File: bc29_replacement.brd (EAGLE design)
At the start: 160 x 100 mm, 4 parts, among them IC1 ATMEGA328P, IC17 CD4070B, J2 2520-5

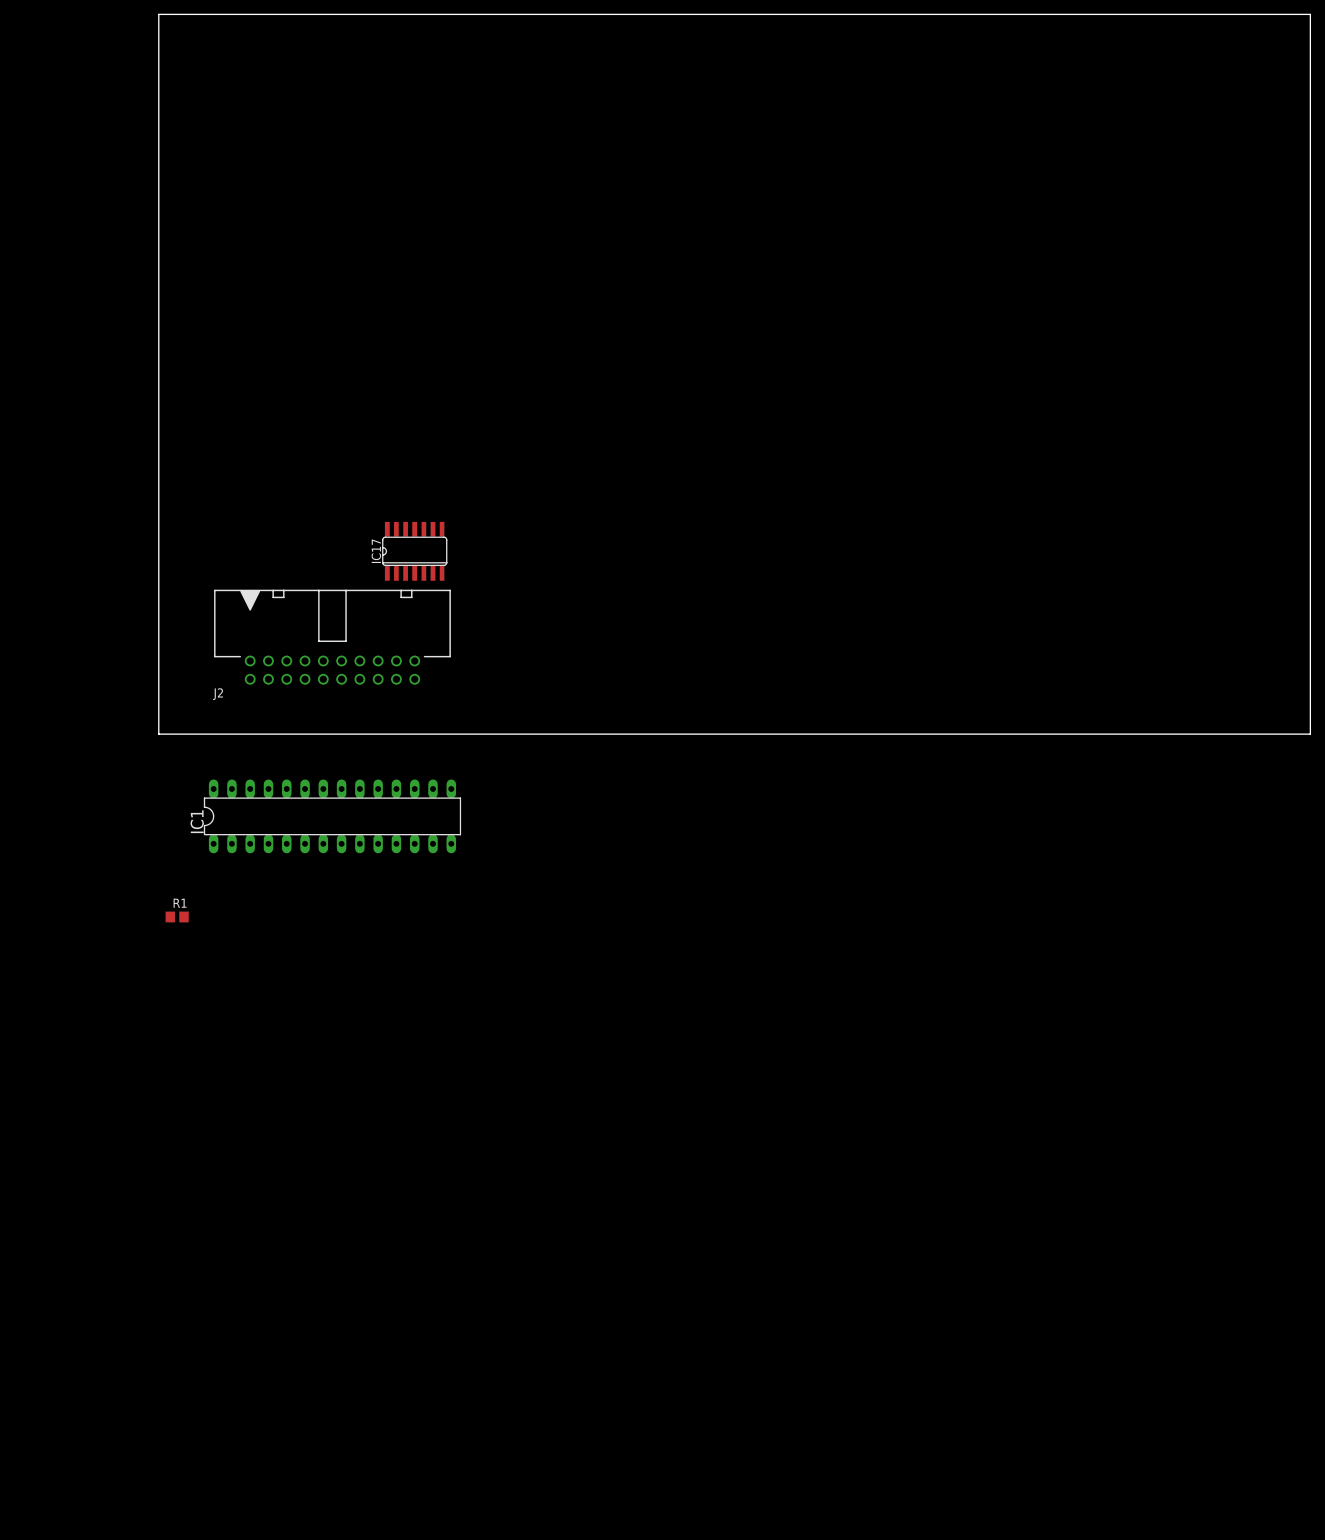
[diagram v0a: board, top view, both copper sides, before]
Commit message: MCU and PCB dimensions
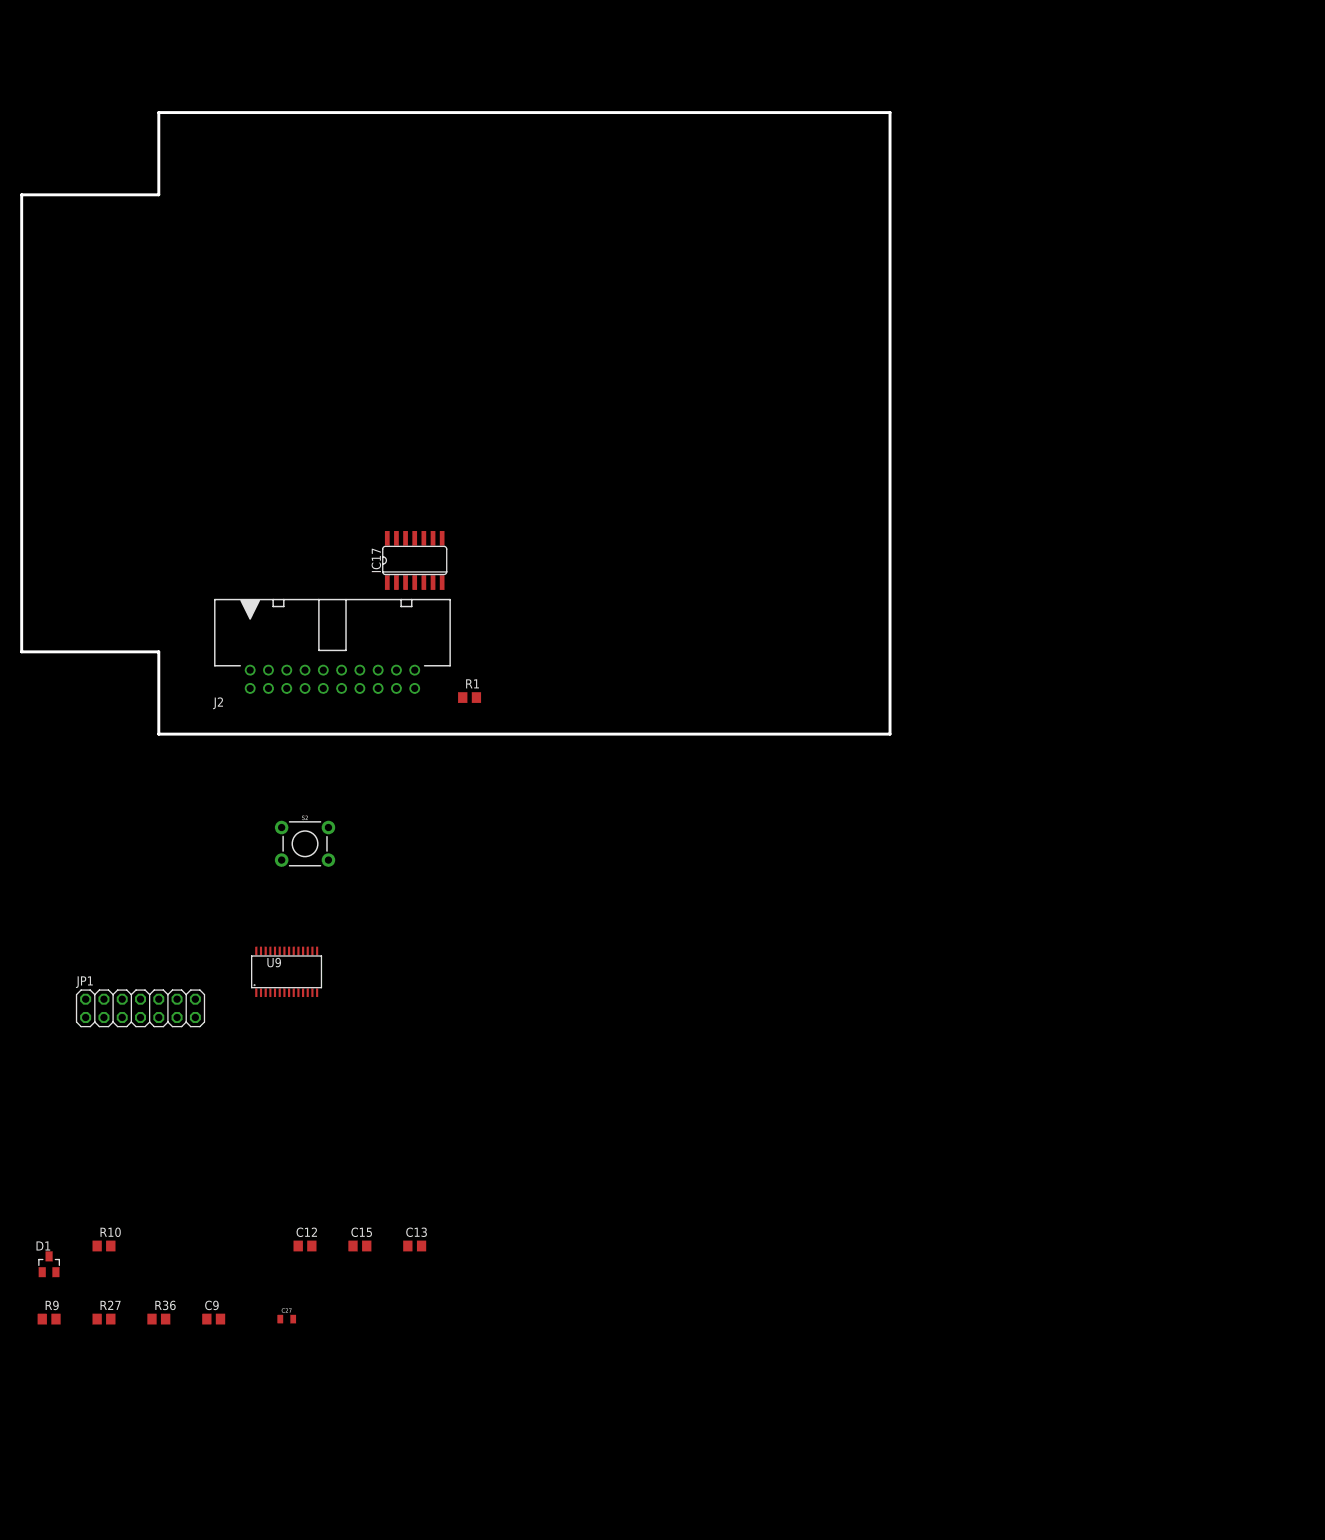
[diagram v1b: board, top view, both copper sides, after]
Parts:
- removed IC1: ATMEGA328P, adafruit:DIL28-3
- added C12: .47uF, rcl:C0805
- added C13: 10uF, rcl:C0805
- added C15: 2.2nF, rcl:C0805
- added C27: 0.1u, SparkFun-Capacitors:0805
- added C9: .1uF, rcl:C0805
- added D1: BAT54, diode:SOT23
- added JP1: JTAG, pinhead:2X07
- added R10: 20.0K, rcl:R0805
- added R27: 0R0, rcl:R0805
- added R36: 300, rcl:R0805
- added R9: 47K, rcl:R0805
- added S2: SPST-PTH-6.0MM, SparkFun-Switches:TACTILE_SWITCH_PTH_6.0MM
- added U9: MSP430I2041TPW, TI_MSP430_v16:PW28
- moved R1 50.8 mm to (43.2, 5.08)
- moved J2 1.27 mm to (24.1, 7.62)
- moved IC17 1.27 mm to (35.6, 24.1)
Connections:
- new net A0.0+: U9.1
- new net A0.0-: U9.2
- new net A1.0+: U9.3
- new net A1.0-: U9.4
- new net A2.0+: U9.5
- new net A2.0-: U9.6
- new net A3.0+: U9.7
- new net A3.0-: U9.8
- new net AGND: C27.2, R10.2, R27.2, U9.10
- new net P1.0: U9.17
- new net P1.1: U9.18
- new net P1.4: U9.21
- new net P1.5: U9.22
- new net P1.6: U9.23
- new net P1.7: U9.24
- new net P2.0: U9.25
- new net P2.1: U9.26
- new net P2.2: U9.27
- new net P2.3: U9.28
- new net ROSC: R10.1, U9.11
- new net RST_JTAG: C15.2, JP1.1, R36.1, R9.1, U9.15
- new net RST_PB: R36.2, S2.3
- new net SBWTCK: JP1.7, U9.16
- new net UCA0RXD: JP1.14, U9.19
- new net UCA0TXD: JP1.12, U9.20
- new net VCC: C13.2, C9.1, D1.3, R9.2, U9.13
- new net VCC_JTAG: D1.1, JP1.2
- new net VCORE: C12.2, U9.14
- new net VREF: C27.1, U9.9
- net GND: now also C12.1, C13.1, C15.1, C9.2, JP1.9, R27.1, S2.1, U9.12
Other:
- board size 160 x 100 mm -> 120.6 x 86.4 mm

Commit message: input network
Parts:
- added C1: 100nF, rcl:C1206
- added C19, C21: 10nF, rcl:C0805
- added C2: 33uF 450V, rcl:E7,5-18
- added C3, C4, C5: 47pF, rcl:C0805
- added D2: P6KEXXC, diode:CB417-15
- added D8: 1N4448, diode:MINIMELF
- added D9: 1N4004, diode:SOD80C
- added E2: 10uF 63V, rcl:E2,5-5
- added E3: 47uf 25V, rcl:E2,5-5
- added F1: 32mA, fuse:FUSE_HOLDER_5X20MM
- added IC18: LP2951, linear:SO08
- added L1: 8mH, inductor-neosid:Z15/4
- added L2, L3: (no value), inductor-neosid:SM-B9
- added M1: IRF740, transistor-power:TO220BV
- added R2, R3: 1.0K, rcl:R0805
- added R29, R30: 1M, rcl:M0805
- added X1: 236-412, con-wago-508:236-412
- added Z1: 12V, diode:SOD80C
- added Z2: 6.2V, diode:SOD80C
- J2: value 2520-5 -> 2520-; device con-3m:PAK100/2500-5-20 -> con-3m:PAK100/2500-20
- moved C12 136.0 mm to (97.8, 40.6)
- moved C13 136.0 mm to (113.0, 40.6)
- moved C15 136.0 mm to (105.4, 40.6)
- moved C27 136.0 mm to (95.2, 30.5)
- moved C9 136.0 mm to (85.1, 30.5)
- moved R10 136.0 mm to (69.8, 40.6)
- moved R27 136.0 mm to (69.8, 30.5)
- moved R36 136.0 mm to (77.5, 30.5)
- moved R9 136.0 mm to (62.2, 30.5)
- moved D1 136.0 mm to (62.2, 38.1)
- moved JP1 136.0 mm to (74.9, 73.7)
- moved U9 136.0 mm to (95.2, 78.7)
- moved S2 75.1 mm to (85.1, 22.9)
- moved J2 22.9 mm to (31.8, 29.2), turned to 90 degrees
- moved IC17 19.0 mm to (54.6, 24.1)
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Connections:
- new net !NAR: X1.5@1
- new net !RESET: X1.7@1
- new net +BATT: F1.1, L1.1, X1.1@1
- new net +BATT_FILT: C2.+, L1.2
- new net 12+: X1.11@1
- new net 12-: X1.12@1
- new net 13V5: D8.A, E2.+, IC18.8, M1.S
- new net AH_NEGATIVE: X1.8@1
- new net DRAIN: D9.C, M1.D
- new net FUSED_BATT+: D9.A, F1.2, R30.2
- new net GATE: C21.1, D8.C, M1.G, R29.2, Z1.C
- new net GND1K: X1.6@1
- new net N$1: D2.C, L2.1
- new net N$2: D2.A, L3.1
- new net N$29: R29.1, R30.1
- new net N$44: IC18.6, IC18.7
- new net N$5: L2.2, R2.2
- new net N$8: L3.2, R3.2
- new net OUT+: X1.9@1
- new net OUT-: X1.10@1
- new net SHUNT+: X1.4@1
- new net SHUNT-: X1.3@1
- net +5V: now also C1.1, C19.1, E3.+, IC18.1, IC18.2, Z1.A, Z2.C
- net A0.0+: now also C4.1, C5.1, R3.1
- net A0.0-: now also C3.2, C5.2, R2.1
- net GND: now also C1.2, C19.2, C2.-, C21.2, C3.1, C4.2, E2.-, E3.-, IC18.4, X1.2@1, Z2.A
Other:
- board size 120.6 x 86.4 mm -> 120.7 x 86.4 mm

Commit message: io expansion
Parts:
- added IC1: 74HCS596D, 74xx-us:SO16
- moved C3 163.5 mm to (108.0, 27.9)
- moved C4 163.5 mm to (108.0, 15.2)
- moved C5 163.5 mm to (108.0, 8.89)
- moved R2 163.5 mm to (108.0, 34.3)
- moved R3 163.5 mm to (108.0, 21.6)
- moved L3 114.1 mm to (95.2, 7.62)
- moved L2 113.1 mm to (94.0, 12.7)
- moved D2 112.5 mm to (96.5, 3.81)
- moved C2 101.1 mm to (33.0, 67.3)
- moved L1 66.3 mm to (27.9, 54.6)
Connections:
- net GND: now also IC1.8
- net VCC: now also IC1.16
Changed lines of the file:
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@@
 <attribute name="MF" value="Wago Corporation" x="6.35" y="71.12" size="1.778" layer="27" rot="R270" display="off"/>
 </element>
-<element name="L1" library="inductor-neosid" package="Z15/4" value="8mH" x="5.08" y="-7.62">
-<attribute name="OC_NEWARK" value="unknown" x="5.08" y="-7.62" size="1.778" layer="27" display="off"/>
-<attribute name="OC_FARNELL" value="unknown" x="5.08" y="-7.62" size="1.778" layer="27" display="off"/>
-<attribute name="MPN" value="" x="5.08" y="-7.62" size="1.778" layer="27" display="off"/>
-<attribute name="MF" value="" x="5.08" y="-7.62" size="1.778" layer="27" display="off"/>
+<element name="L1" library="inductor-neosid" package="Z15/4" value="8mH" x="27.94" y="54.61">
+<attribute name="OC_NEWARK" value="unknown" x="27.94" y="54.61" size="1.778" layer="27" display="off"/>
+<attribute name="OC_FARNELL" value="unknown" x="27.94" y="54.61" size="1.778" layer="27" display="off"/>
+<attribute name="MPN" value="" x="27.94" y="54.61" size="1.778" layer="27" display="off"/>
+<attribute name="MF" value="" x="27.94" y="54.61" size="1.778" layer="27" display="off"/>
 </element>
-<element name="C2" library="rcl" package="E7,5-18" value="33uF 450V" x="12.7" y="-31.75"/>
-<element name="L2" library="inductor-neosid" package="SM-B9" value="" x="1.27" y="-52.07">
-<attribute name="OC_NEWARK" value="unknown" x="1.27" y="-52.07" size="1.778" layer="27" display="off"/>
-<attribute name="OC_FARNELL" value="unknown" x="1.27" y="-52.07" size="1.778" layer="27" display="off"/>
-<attribute name="MPN" value="" x="1.27" y="-52.07" size="1.778" layer="27" display="off"/>
-<attribute name="MF" value="" x="1.27" y="-52.07" size="1.778" layer="27" display="off"/>
+<element name="C2" library="rcl" package="E7,5-18" value="33uF 450V" x="33.02" y="67.31"/>
+<element name="L2" library="inductor-neosid" package="SM-B9" value="" x="93.98" y="12.7">
+<attribute name="OC_NEWARK" value="unknown" x="93.98" y="12.7" size="1.778" layer="27" display="off"/>
+<attribute name="OC_FARNELL" value="unknown" x="93.98" y="12.7" size="1.778" layer="27" display="off"/>
+<attribute name="MPN" value="" x="93.98" y="12.7" size="1.778" layer="27" display="off"/>
+<attribute name="MF" value="" x="93.98" y="12.7" size="1.778" layer="27" display="off"/>
 </element>
-<element name="L3" library="inductor-neosid" package="SM-B9" value="" x="1.27" y="-57.15">
-<attribute name="OC_NEWARK" value="unknown" x="1.27" y="-57.15" size="1.778" layer="27" display="off"/>
-<attribute name="OC_FARNELL" value="unknown" x="1.27" y="-57.15" size="1.778" layer="27" display="off"/>
-<attribute name="MPN" value="" x="1.27" y="-57.15" size="1.778" layer="27" display="off"/>
-<attribute name="MF" value="" x="1.27" y="-57.15" size="1.778" layer="27" display="off"/>
+<element name="L3" library="inductor-neosid" package="SM-B9" value="" x="95.25" y="7.62">
+<attribute name="OC_NEWARK" value="unknown" x="95.25" y="7.62" size="1.778" layer="27" display="off"/>
+<attribute name="OC_FARNELL" value="unknown" x="95.25" y="7.62" size="1.778" layer="27" display="off"/>
+<attribute name="MPN" value="" x="95.25" y="7.62" size="1.778" layer="27" display="off"/>
+<attribute name="MF" value="" x="95.25" y="7.62" size="1.778" layer="27" display="off"/>
 </element>
-<element name="D2" library="diode" package="CB417-15" value="P6KEXXC" x="11.43" y="-69.85"/>
-<element name="C3" library="rcl" package="C0805" value="47pF" x="-5.08" y="-90.17"/>
-<element name="R2" library="rcl" package="R0805" value="1.0K " x="-5.08" y="-83.82"/>
-<element name="R3" library="rcl" package="R0805" value="1.0K " x="-5.08" y="-96.52"/>
-<element name="C4" library="rcl" package="C0805" value="47pF" x="-5.08" y="-102.87"/>
-<element name="C5" library="rcl" package="C0805" value="47pF" x="-5.08" y="-109.22"/>
+<element name="D2" library="diode" package="CB417-15" value="P6KEXXC" x="96.52" y="3.81"/>
+<element name="C3" library="rcl" package="C0805" value="47pF" x="107.95" y="27.94"/>
+<element name="R2" library="rcl" package="R0805" value="1.0K " x="107.95" y="34.29"/>
+<element name="R3" library="rcl" package="R0805" value="1.0K " x="107.95" y="21.59"/>
+<element name="C4" library="rcl" package="C0805" value="47pF" x="107.95" y="15.24"/>
+<element name="C5" library="rcl" package="C0805" value="47pF" x="107.95" y="8.89"/>
+<element name="IC1" library="74xx-us" package="SO16" value="74HCS596D" x="97.79" y="55.88"/>
 </elements>
 <signals>
@@
 <contactref element="C3" pad="1"/>
 <contactref element="C4" pad="2"/>
+<contactref element="IC1" pad="8"/>
 <wire x1="77.47" y1="72.39" x2="98.1711" y2="75.832" width="0" layer="19" extent="1-1"/>
 <wire x1="73.66" y1="68.58" x2="77.47" y2="72.39" width="0" layer="19" extent="1-1"/>
@@
 <wire x1="104.46" y1="40.64" x2="96.84" y2="40.64" width="0" layer="19" extent="1-1"/>
 <wire x1="112.08" y1="40.64" x2="104.46" y2="40.64" width="0" layer="19" extent="1-1"/>
+<wire x1="107" y1="27.94" x2="104.46" y2="40.64" width="0" layer="19" extent="1-1"/>
+<wire x1="108.9" y1="15.24" x2="107" y2="27.94" width="0" layer="19" extent="1-1"/>
 <wire x1="68.9" y1="30.48" x2="81.8388" y2="25.1206" width="0" layer="19" extent="1-1"/>
 <wire x1="58.42" y1="21.0566" x2="68.9" y2="30.48" width="0" layer="19" extent="1-1"/>
 <wire x1="50.8" y1="68.58" x2="73.66" y2="68.58" width="0" layer="19" extent="1-1"/>
+<wire x1="36.83" y1="67.31" x2="50.8" y2="68.58" width="0" layer="19" extent="1-1"/>
 <wire x1="42.86" y1="38.1" x2="58.42" y2="21.0566" width="0" layer="19" extent="1-1"/>
 <wire x1="33.02" y1="22.86" x2="42.86" y2="38.1" width="0" layer="19" extent="1-1"/>
-<wire x1="3.81" y1="66.04" x2="50.8" y2="68.58" width="0" layer="19" extent="1-1"/>
-<wire x1="16.51" y1="-31.75" x2="33.02" y2="22.86" width="0" layer="19" extent="1-1"/>
-<wire x1="-6.03" y1="-90.17" x2="16.51" y2="-31.75" width="0" layer="19" extent="1-1"/>
-<wire x1="-4.13" y1="-102.87" x2="-6.03" y2="-90.17" width="0" layer="19" extent="1-1"/>
+<wire x1="3.81" y1="66.04" x2="36.83" y2="67.31" width="0" layer="19" extent="1-1"/>
+<wire x1="102.235" y1="52.8066" x2="33.02" y2="22.86" width="0" layer="19" extent="1-1"/>
 </signal>
 <signal name="+5V">
@@
 <contactref element="R9" pad="2"/>
 <contactref element="D1" pad="3"/>
+<contactref element="IC1" pad="16"/>
+<wire x1="113.98" y1="40.64" x2="98.8211" y2="75.832" width="0" layer="19" extent="1-1"/>
+<wire x1="84.14" y1="30.48" x2="113.98" y2="40.64" width="0" layer="19" extent="1-1"/>
+<wire x1="63.18" y1="30.48" x2="84.14" y2="30.48" width="0" layer="19" extent="1-1"/>
 <wire x1="62.23" y1="39.2" x2="63.18" y2="30.48" width="0" layer="19" extent="1-1"/>
-<wire x1="84.14" y1="30.48" x2="63.18" y2="30.48" width="0" layer="19" extent="1-1"/>
-<wire x1="113.98" y1="40.64" x2="84.14" y2="30.48" width="0" layer="19" extent="1-1"/>
-<wire x1="98.8211" y1="75.832" x2="113.98" y2="40.64" width="0" layer="19" extent="1-1"/>
+<wire x1="93.345" y1="58.9534" x2="63.18" y2="30.48" width="0" layer="19" extent="1-1"/>
 </signal>
 <signal name="UCA0TXD">
@@
 <contactref element="C4" pad="1"/>
 <contactref element="C5" pad="1"/>
-<wire x1="-6.03" y1="-96.52" x2="91.021" y2="75.832" width="0" layer="19" extent="1-1"/>
-<wire x1="-6.03" y1="-102.87" x2="-6.03" y2="-96.52" width="0" layer="19" extent="1-1"/>
-<wire x1="-6.03" y1="-109.22" x2="-6.03" y2="-102.87" width="0" layer="19" extent="1-1"/>
+<wire x1="107" y1="21.59" x2="91.021" y2="75.832" width="0" layer="19" extent="1-1"/>
+<wire x1="107" y1="15.24" x2="107" y2="21.59" width="0" layer="19" extent="1-1"/>
+<wire x1="107" y1="8.89" x2="107" y2="15.24" width="0" layer="19" extent="1-1"/>
 </signal>
 <signal name="A0.0-">
@@
 <contactref element="C3" pad="2"/>
 <contactref element="C5" pad="2"/>
-<wire x1="-6.03" y1="-83.82" x2="91.671" y2="75.832" width="0" layer="19" extent="1-1"/>
-<wire x1="-4.13" y1="-90.17" x2="-6.03" y2="-83.82" width="0" layer="19" extent="1-1"/>
-<wire x1="-4.13" y1="-109.22" x2="-4.13" y2="-90.17" width="0" layer="19" extent="1-1"/>
+<wire x1="107" y1="34.29" x2="91.671" y2="75.832" width="0" layer="19" extent="1-1"/>
+<wire x1="108.9" y1="27.94" x2="107" y2="34.29" width="0" layer="19" extent="1-1"/>
+<wire x1="108.9" y1="8.89" x2="108.9" y2="27.94" width="0" layer="19" extent="1-1"/>
 </signal>
 <signal name="A1.0+">
@@
 <contactref element="L1" pad="1"/>
 <wire x1="3.81" y1="71.12" x2="41.91" y2="80.01" width="0" layer="19" extent="1-1"/>
-<wire x1="-0.92" y1="-9.42" x2="3.81" y2="71.12" width="0" layer="19" extent="1-1"/>
+<wire x1="21.94" y1="52.81" x2="3.81" y2="71.12" width="0" layer="19" extent="1-1"/>
 </signal>
 <signal name="FUSED_BATT+">
@@
 <contactref element="L1" pad="2"/>
 <contactref element="C2" pad="+"/>
-<wire x1="11.08" y1="-5.82" x2="8.89" y2="-31.75" width="0" layer="19" extent="1-1"/>
+<wire x1="33.94" y1="56.41" x2="29.21" y2="67.31" width="0" layer="19" extent="1-1"/>
 </signal>
 <signal name="N$1">
 <contactref element="D2" pad="C"/>
 <contactref element="L2" pad="1"/>
-<wire x1="-2.73" y1="-52.07" x2="3.81" y2="-69.85" width="0" layer="19" extent="1-1"/>
+<wire x1="89.98" y1="12.7" x2="88.9" y2="3.81" width="0" layer="19" extent="1-1"/>
 </signal>
 <signal name="N$2">
 <contactref element="D2" pad="A"/>
 <contactref element="L3" pad="1"/>
-<wire x1="19.05" y1="-69.85" x2="-2.73" y2="-57.15" width="0" layer="19" extent="1-1"/>
+<wire x1="104.14" y1="3.81" x2="91.25" y2="7.62" width="0" layer="19" extent="1-1"/>
 </signal>
 <signal name="N$5">
 <contactref element="L2" pad="2"/>
 <contactref element="R2" pad="2"/>
-<wire x1="5.27" y1="-52.07" x2="-4.13" y2="-83.82" width="0" layer="19" extent="1-1"/>
+<wire x1="97.98" y1="12.7" x2="108.9" y2="34.29" width="0" layer="19" extent="1-1"/>
 </signal>
 <signal name="N$8">
 <contactref element="L3" pad="2"/>
 <contactref element="R3" pad="2"/>
-<wire x1="5.27" y1="-57.15" x2="-4.13" y2="-96.52" width="0" layer="19" extent="1-1"/>
+<wire x1="99.25" y1="7.62" x2="108.9" y2="21.59" width="0" layer="19" extent="1-1"/>
 </signal>
 </signals>
